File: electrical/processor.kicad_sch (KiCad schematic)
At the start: 0 parts

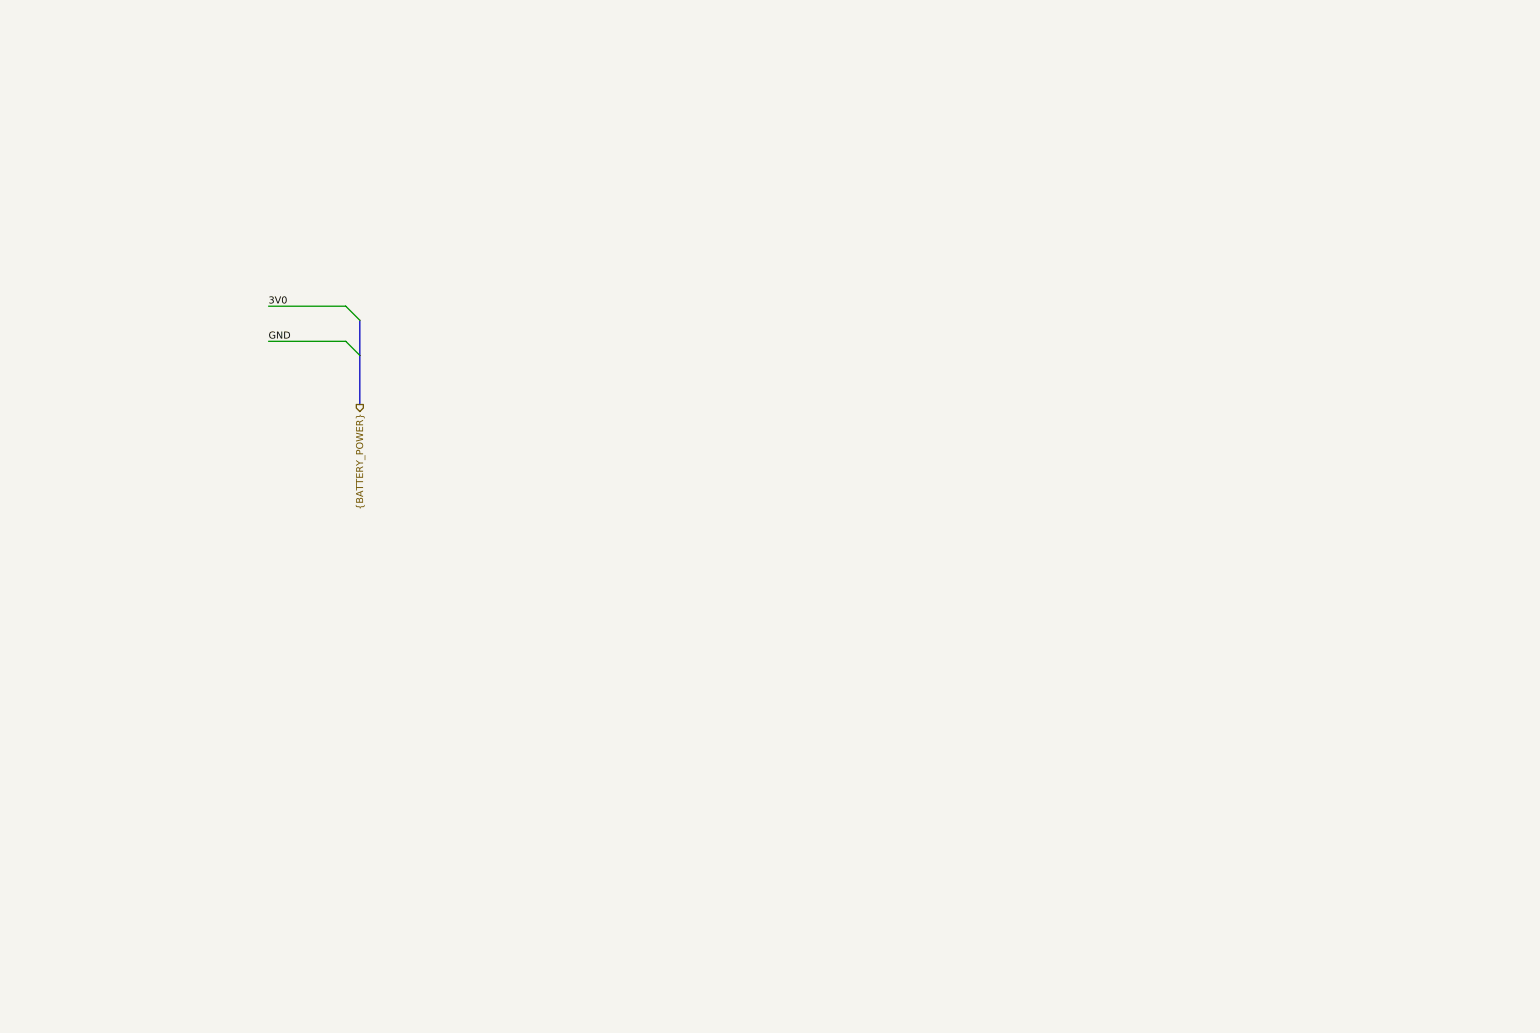
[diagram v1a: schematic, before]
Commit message: #3 Implementing base schematic for processor.
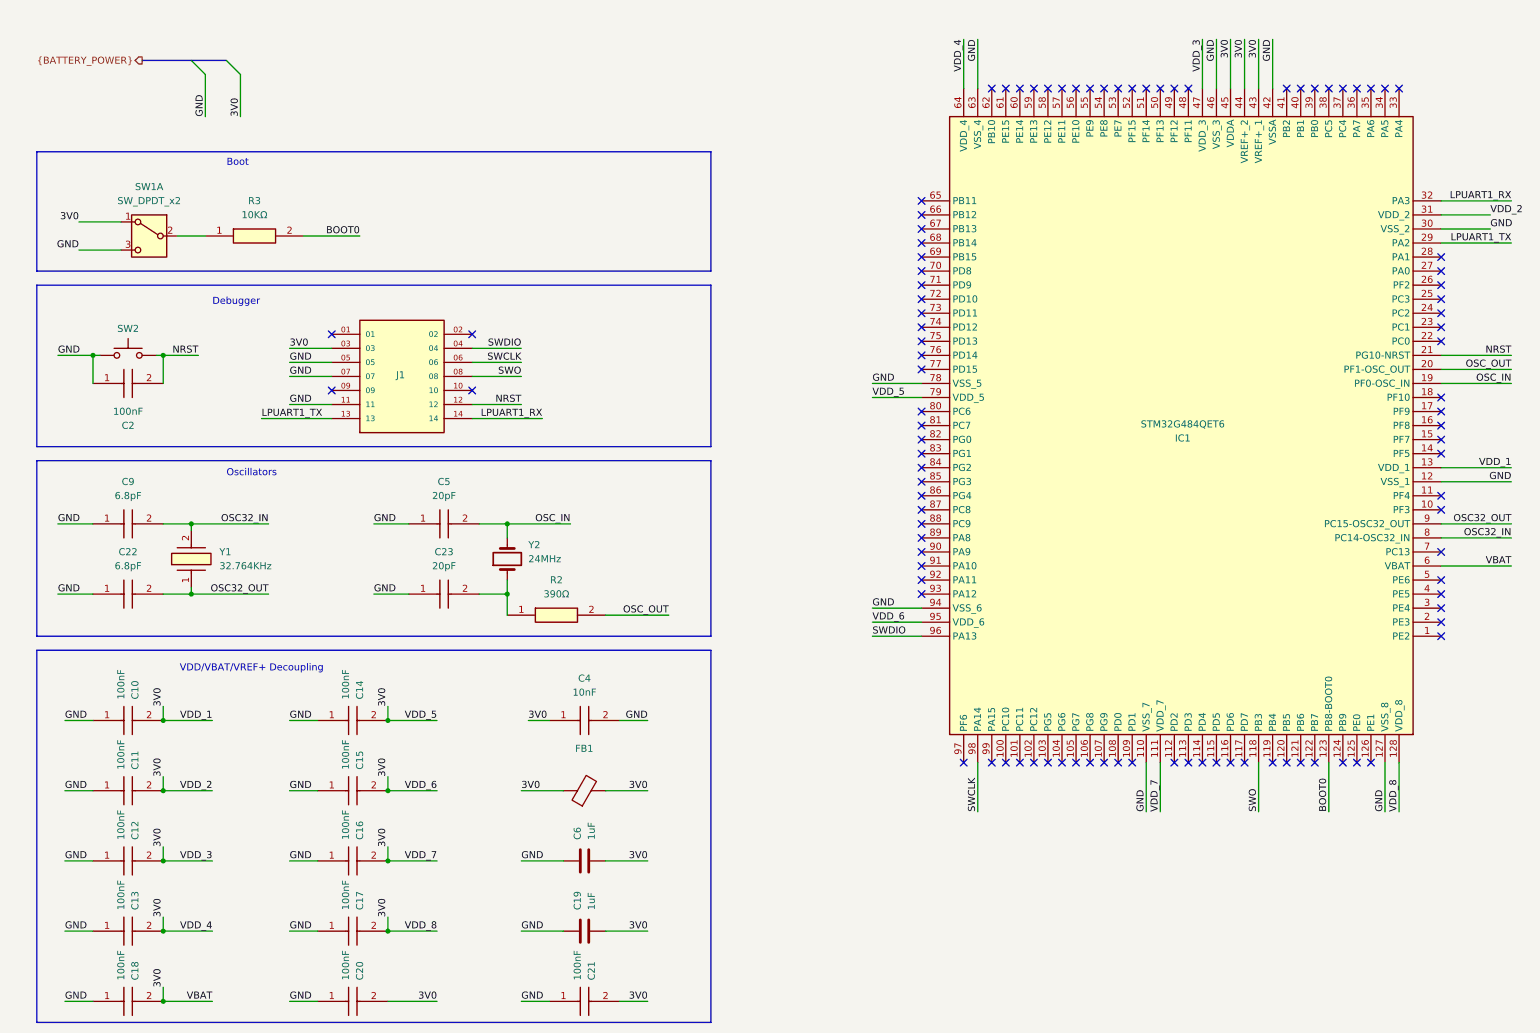
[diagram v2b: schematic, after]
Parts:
- added C10, C11, C12, C13, C14, C15, C16, C17, C18, C2, C20, C21: 100nF, SamacSys_Parts:MAJx16, symbol SamacSys_Parts:MAJCH168BB7104KTEA01
- added C19, C6: 1uF, symbol Device:C
- added C22, C9: 6.8pF, SamacSys_Parts:CAPC1608X90N, symbol SamacSys_Parts:0603YA6R8CAT2A
- added C23, C5: 20pF, SamacSys_Parts:CAPC1608X90N, symbol SamacSys_Parts:06031A200KAT2A
- added C4: 10nF, SamacSys_Parts:CAPC1608X90N, symbol SamacSys_Parts:06035A103JAT2A
- added FB1: FerriteBead, symbol Device:FerriteBead
- added IC1: STM32G484QET6, SamacSys_Parts:QFP40P1600X1600X160-128N, symbol SamacSys_Parts:STM32G484QET6
- added J1: FTSH-107-01-F-DV-K, FTSH-107-01-F-DV-K:SAMTEC_FTSH-107-01-F-DV-K, symbol FTSH-107-01-F-DV-K:FTSH-107-01-F-DV-K
- added R2: 390Ω, SamacSys_Parts:RESC1608X58N, symbol SamacSys_Parts:MCT0603MD3900BP500
- added R3: 10KΩ, SamacSys_Parts:RESC1608X58N, symbol SamacSys_Parts:RA73F1J10KBTDF
- added SW1: SW_DPDT_x2, symbol Switch:SW_DPDT_x2
- added SW2: SW_Push, symbol Switch:SW_Push
- added Y1: 32.764KHz, SamacSys_Parts:XT1312HHRXX32K76E, symbol SamacSys_Parts:XT1312HHRXX32K76E
- added Y2: 24MHz, symbol Device:Crystal
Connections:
- net 3V0: now also C10.2, C11.2, C12.2, C13.2, C14.2, C15.2, C16.2, C17.2, C18.2, C19.2, C20.2, C21.2, C4.1, C6.2, FB1.1, FB1.2, IC1.111 (VDD_7), IC1.128 (VDD_8), IC1.13 (VDD_1), IC1.31 (VDD_2), IC1.43 (VREF+_1), IC1.44 (VREF+_2), IC1.45 (VDDA), IC1.47 (VDD_3), IC1.6 (VBAT), IC1.64 (VDD_4), IC1.79 (VDD_5), IC1.95 (VDD_6), J1.03, SW1.1 (A)
- net GND: now also C10.1, C11.1, C12.1, C13.1, C14.1, C15.1, C16.1, C17.1, C18.1, C19.1, C2.1, C20.1, C21.1, C22.1, C23.1, C4.2, C5.1, C6.1, C9.1, IC1.110 (VSS_7), IC1.12 (VSS_1), IC1.127 (VSS_8), IC1.30 (VSS_2), IC1.42 (VSSA), IC1.46 (VSS_3), IC1.63 (VSS_4), IC1.78 (VSS_5), IC1.94 (VSS_6), J1.05, J1.07, J1.11, SW1.3 (C), SW2.1
- new net: C23.2, R2.1, Y2.1
- new net: R3.1, SW1.2 (B)
- new net BOOT0: IC1.123 (PB8-BOOT0), R3.2
- new net LPUART1_RX: IC1.32 (PA3), J1.14
- new net LPUART1_TX: IC1.29 (PA2), J1.13
- new net NRST: C2.2, IC1.21 (PG10-NRST), J1.12, SW2.2
- new net OSC32_IN: C9.2, IC1.8 (PC14-OSC32_IN), Y1.2
- new net OSC32_OUT: C22.2, IC1.9 (PC15-OSC32_OUT), Y1.1
- new net OSC_IN: C5.2, IC1.19 (PF0-OSC_IN), Y2.2
- new net OSC_OUT: IC1.20 (PF1-OSC_OUT), R2.2
- new net SWCLK: IC1.98 (PA14), J1.06
- new net SWDIO: IC1.96 (PA13), J1.04
- new net SWO: IC1.118 (PB3), J1.08
- no-connect marks 0 -> 100
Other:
- note added: "Boot"
- note added: "Debugger"
- note added: "Oscillators"
- note added: "VDD/VBAT/VREF+ Decoupling"
- company: (none) -> AlumaPower
- title: (none) -> Etchasketch - Processor

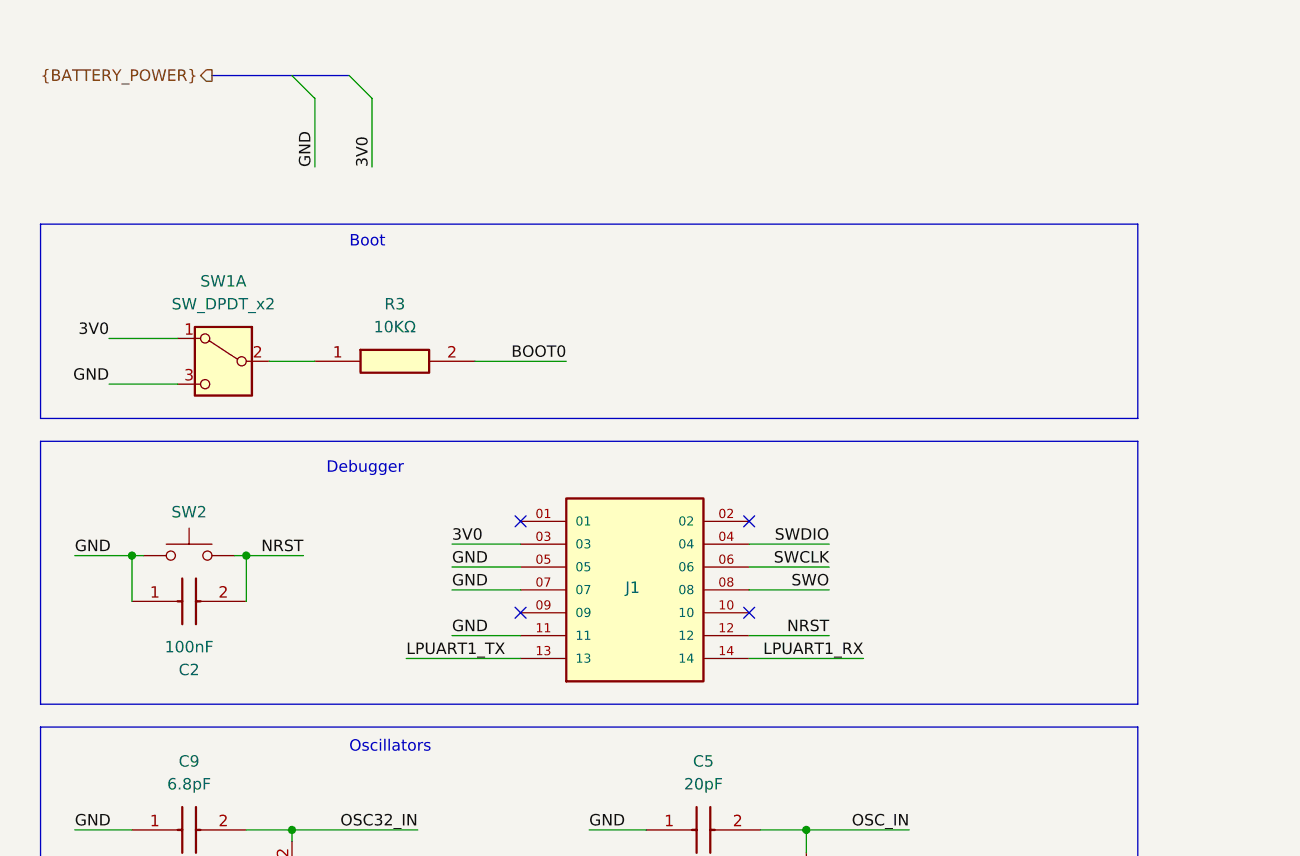
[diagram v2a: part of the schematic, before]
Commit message: #3 Implementing potentionometers and  beginning IOC file creation.
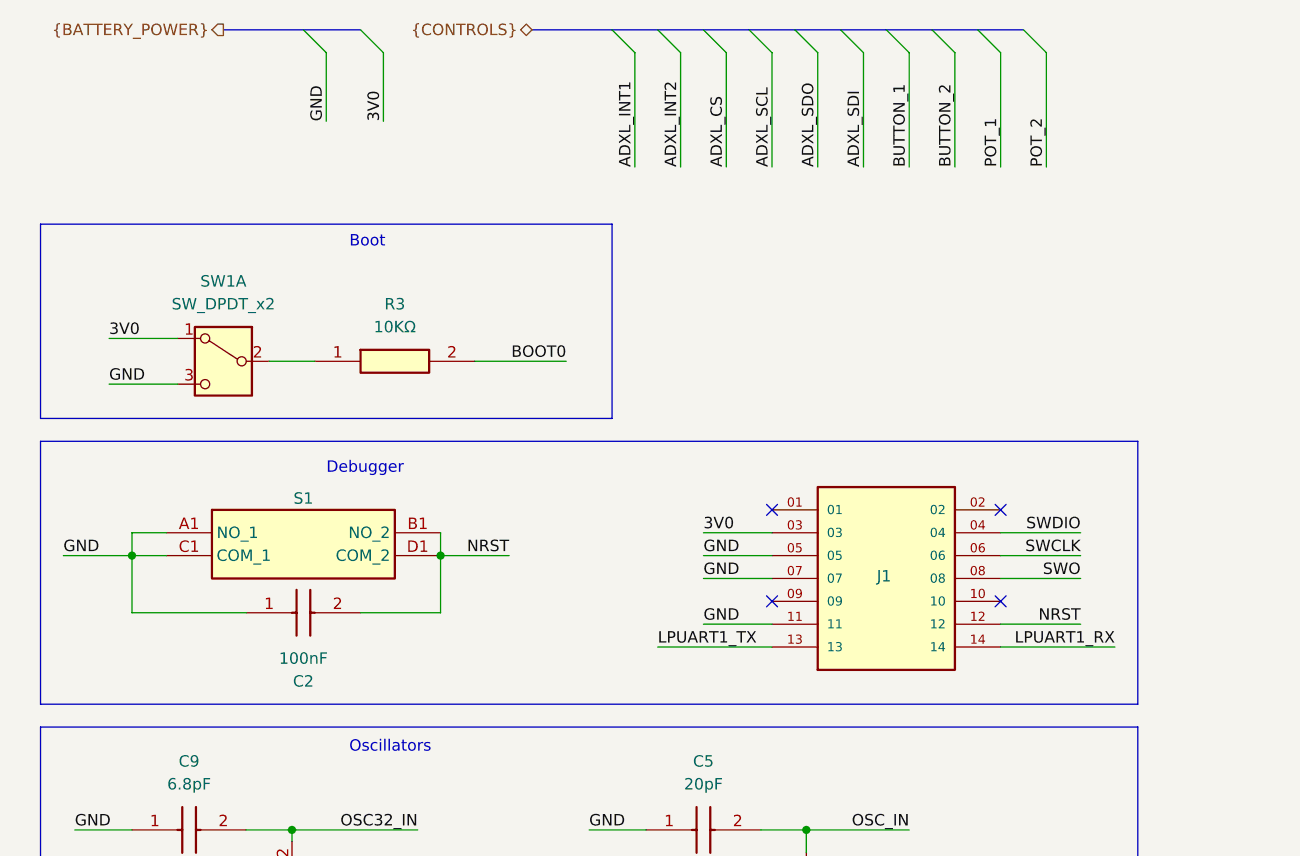
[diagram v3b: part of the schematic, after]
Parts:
- removed SW2: SW_Push, symbol Switch:SW_Push
- added S1: PTS125SM73SMTR21M_LFS, SamacSys_Parts:PTS125SM73SMTR21MLFS, symbol SamacSys_Parts:PTS125SM73SMTR21M_LFS
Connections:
- net GND: now also S1.A1 (NO_1), S1.C1 (COM_1)
- net NRST: now also S1.B1 (NO_2), S1.D1 (COM_2)
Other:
- moved on the sheet: C2, J1

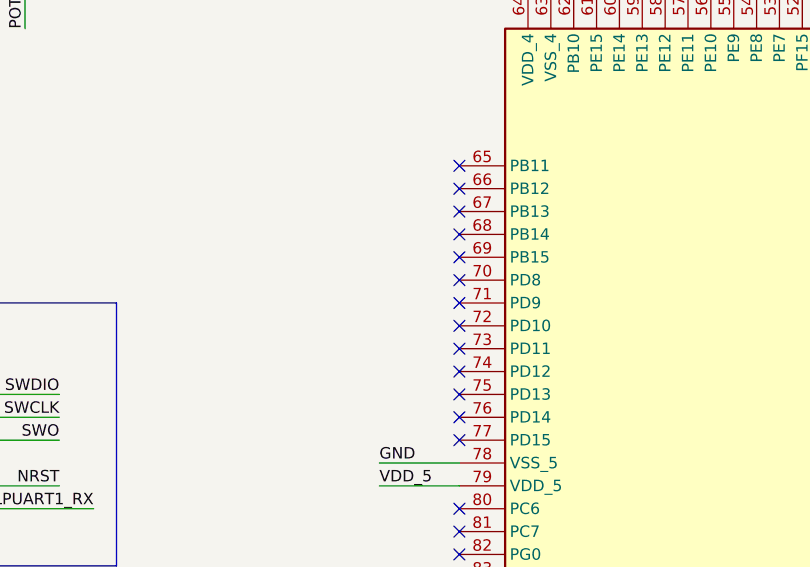
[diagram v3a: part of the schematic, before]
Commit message: #3 Adding controls connections to STM32, updating IOC file to match.
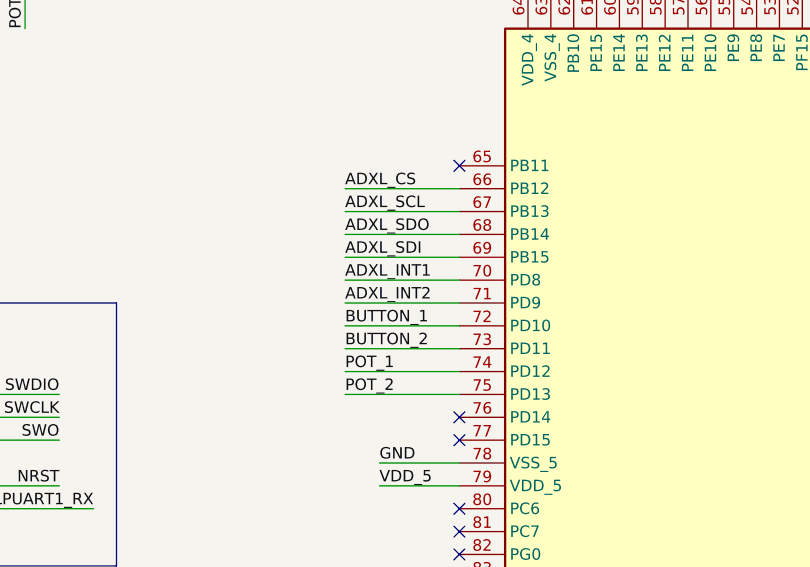
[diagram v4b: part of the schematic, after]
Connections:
- net ADXL_CS: now also IC1.66 (PB12)
- net ADXL_INT1: now also IC1.70 (PD8)
- net ADXL_INT2: now also IC1.71 (PD9)
- net ADXL_SCL: now also IC1.67 (PB13)
- net ADXL_SDI: now also IC1.69 (PB15)
- net ADXL_SDO: now also IC1.68 (PB14)
- net BUTTON_1: now also IC1.72 (PD10)
- net BUTTON_2: now also IC1.73 (PD11)
- net POT_1: now also IC1.74 (PD12)
- net POT_2: now also IC1.75 (PD13)
- no-connect marks 100 -> 90
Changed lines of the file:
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@@
-	)
-	(no_connect
-		(at 173.99 73.66)
 	)
 	(no_connect
@@
 	)
 	(no_connect
-		(at 173.99 60.96)
-	)
-	(no_connect
 		(at 252.73 27.94)
 	)
@@
 	)
 	(no_connect
-		(at 173.99 68.58)
-	)
-	(no_connect
 		(at 252.73 149.86)
 	)
 	(no_connect
-		(at 173.99 55.88)
-	)
-	(no_connect
 		(at 173.99 111.76)
 	)
@@
 	)
 	(no_connect
-		(at 173.99 50.8)
-	)
-	(no_connect
 		(at 267.97 116.84)
 	)
 	(no_connect
-		(at 173.99 71.12)
-	)
-	(no_connect
 		(at 189.23 27.94)
 	)
@@
 	)
 	(no_connect
-		(at 173.99 66.04)
-	)
-	(no_connect
-		(at 173.99 58.42)
-	)
-	(no_connect
 		(at 173.99 86.36)
 	)
 	(no_connect
-		(at 173.99 63.5)
-	)
-	(no_connect
 		(at 173.99 116.84)
 	)
@@
 	(no_connect
 		(at 173.99 93.98)
-	)
-	(no_connect
-		(at 173.99 53.34)
 	)
 	(no_connect
@@
 	(wire
 		(pts
+			(xy 161.29 63.5) (xy 173.99 63.5)
+		)
+		(stroke
+			(width 0)
+			(type default)
+		)
+	)
+	(wire
+		(pts
 			(xy 19.05 154.94) (xy 24.13 154.94)
 		)
@@
 	(wire
 		(pts
+			(xy 161.29 55.88) (xy 173.99 55.88)
+		)
+		(stroke
+			(width 0)
+			(type default)
+		)
+	)
+	(wire
+		(pts
 			(xy 267.97 78.74) (xy 280.67 78.74)
 		)
@@
 		)
 	)
+	(wire
+		(pts
+			(xy 161.29 53.34) (xy 173.99 53.34)
+		)
+		(stroke
+			(width 0)
+			(type default)
+		)
+	)
 	(polyline
 		(pts
@@
 		)
 	)
+	(wire
+		(pts
+			(xy 161.29 68.58) (xy 173.99 68.58)
+		)
+		(stroke
+			(width 0)
+			(type default)
+		)
+	)
 	(bus
 		(pts
@@
 	(wire
 		(pts
+			(xy 161.29 73.66) (xy 173.99 73.66)
+		)
+		(stroke
+			(width 0)
+			(type default)
+		)
+	)
+	(wire
+		(pts
 			(xy 58.42 76.2) (xy 66.04 76.2)
 		)
@@
 	(wire
 		(pts
+			(xy 161.29 60.96) (xy 173.99 60.96)
+		)
+		(stroke
+			(width 0)
+			(type default)
+		)
+	)
+	(wire
+		(pts
 			(xy 165.1 121.92) (xy 173.99 121.92)
 		)
@@
 	(wire
 		(pts
+			(xy 161.29 71.12) (xy 173.99 71.12)
+		)
+		(stroke
+			(width 0)
+			(type default)
+		)
+	)
+	(wire
+		(pts
 			(xy 17.78 106.68) (xy 24.13 106.68)
 		)
@@
 	(wire
 		(pts
+			(xy 161.29 58.42) (xy 173.99 58.42)
+		)
+		(stroke
+			(width 0)
+			(type default)
+		)
+	)
+	(wire
+		(pts
 			(xy 99.06 119.38) (xy 99.06 116.84)
 		)
@@
 	(wire
 		(pts
+			(xy 161.29 66.04) (xy 173.99 66.04)
+		)
+		(stroke
+			(width 0)
+			(type default)
+		)
+	)
+	(wire
+		(pts
 			(xy 77.47 167.64) (xy 77.47 165.1)
 		)
@@
 		(pts
 			(xy 13.97 60.96) (xy 13.97 39.37)
+		)
+		(stroke
+			(width 0)
+			(type default)
+		)
+	)
+	(wire
+		(pts
+			(xy 161.29 50.8) (xy 173.99 50.8)
 		)
 		(stroke
@@
 		)
 	)
+	(label "ADXL_CS"
+		(at 161.29 50.8 0)
+		(effects
+			(font
+				(size 1.27 1.27)
+			)
+			(justify left bottom)
+		)
+	)
 	(label "VDD_5"
 		(at 165.1 83.82 0)
@@
 		)
 	)
+	(label "ADXL_SDI"
+		(at 161.29 58.42 0)
+		(effects
+			(font
+				(size 1.27 1.27)
+			)
+			(justify left bottom)
+		)
+	)
 	(label "BOOT0"
 		(at 72.39 54.61 180)
@@
 		)
 	)
+	(label "BUTTON_2"
+		(at 161.29 68.58 0)
+		(effects
+			(font
+				(size 1.27 1.27)
+			)
+			(justify left bottom)
+		)
+	)
 	(label "GND"
 		(at 257.81 158.75 90)
+		(effects
+			(font
+				(size 1.27 1.27)
+			)
+			(justify left bottom)
+		)
+	)
+	(label "POT_1"
+		(at 161.29 71.12 0)
 		(effects
 			(font
@@
 		)
 	)
+	(label "ADXL_SDO"
+		(at 161.29 55.88 0)
+		(effects
+			(font
+				(size 1.27 1.27)
+			)
+			(justify left bottom)
+		)
+	)
 	(label "3V0"
 		(at 232.41 19.05 270)
@@
 		)
 	)
+	(label "ADXL_SCL"
+		(at 161.29 53.34 0)
+		(effects
+			(font
+				(size 1.27 1.27)
+			)
+			(justify left bottom)
+		)
+	)
 	(label "NRST"
 		(at 129.54 83.82 180)
@@
 		)
 	)
+	(label "BUTTON_1"
+		(at 161.29 66.04 0)
+		(effects
+			(font
+				(size 1.27 1.27)
+			)
+			(justify left bottom)
+		)
+	)
 	(label "GND"
 		(at 74.93 106.68 0)
@@
 		)
 	)
+	(label "ADXL_INT2"
+		(at 161.29 63.5 0)
+		(effects
+			(font
+				(size 1.27 1.27)
+			)
+			(justify left bottom)
+		)
+	)
 	(label "GND"
 		(at 19.05 142.24 0)
@@
 		)
 	)
+	(label "POT_2"
+		(at 161.29 73.66 0)
+		(effects
+			(font
+				(size 1.27 1.27)
+			)
+			(justify left bottom)
+		)
+	)
 	(label "LPUART1_RX"
 		(at 280.67 48.26 180)
@@
 		(effects
 			(font
+				(size 1.27 1.27)
+			)
+			(justify left bottom)
+		)
+	)
+	(label "ADXL_INT1"
+		(at 161.29 60.96 0)
+		(effects
+			(font
